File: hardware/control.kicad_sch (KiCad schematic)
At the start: 8 parts, among them U1 STM32G0C1KCTxN

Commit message: values-correction
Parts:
- C1, C3: value 100nF -> 100n
- C6: value 10uF -> 10u
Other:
- note removed: "MISO MOSI SCK? PWM: PWM1-TIM_CH3, PWM2-TIM_CH4? LED?"
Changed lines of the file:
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@@
-		)
-	)
-	(text "MISO MOSI SCK?\nPWM: PWM1-TIM_CH3, PWM2-TIM_CH4?\nLED?"
-		(exclude_from_sim no)
-		(at 193.04 88.646 0)
-		(effects
-			(font
-				(size 1.27 1.27)
-			)
 		)
 	)
@@
 			)
 		)
-		(property "Value" "10uF"
+		(property "Value" "10u"
 			(at 73.66 50.8063 0)
 			(effects
@@
 			)
 		)
-		(property "Value" "100nF"
+		(property "Value" "100n"
 			(at 85.09 50.8063 0)
 			(effects
@@
 			)
 		)
-		(property "Value" "100nF"
+		(property "Value" "100n"
 			(at 110.49 50.8062 0)
 			(effects

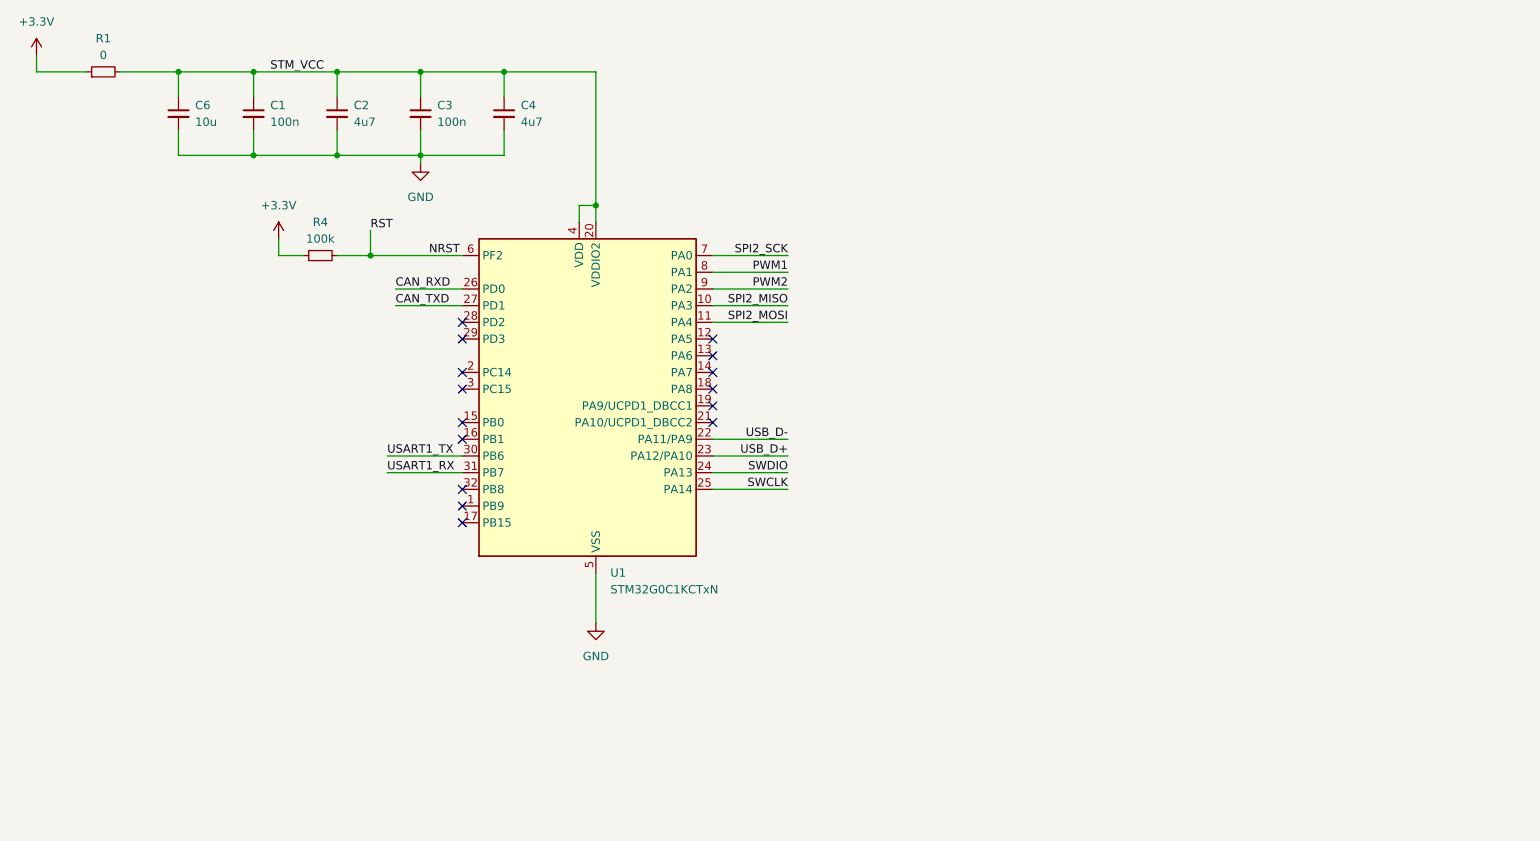
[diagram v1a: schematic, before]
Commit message: added sheet pins
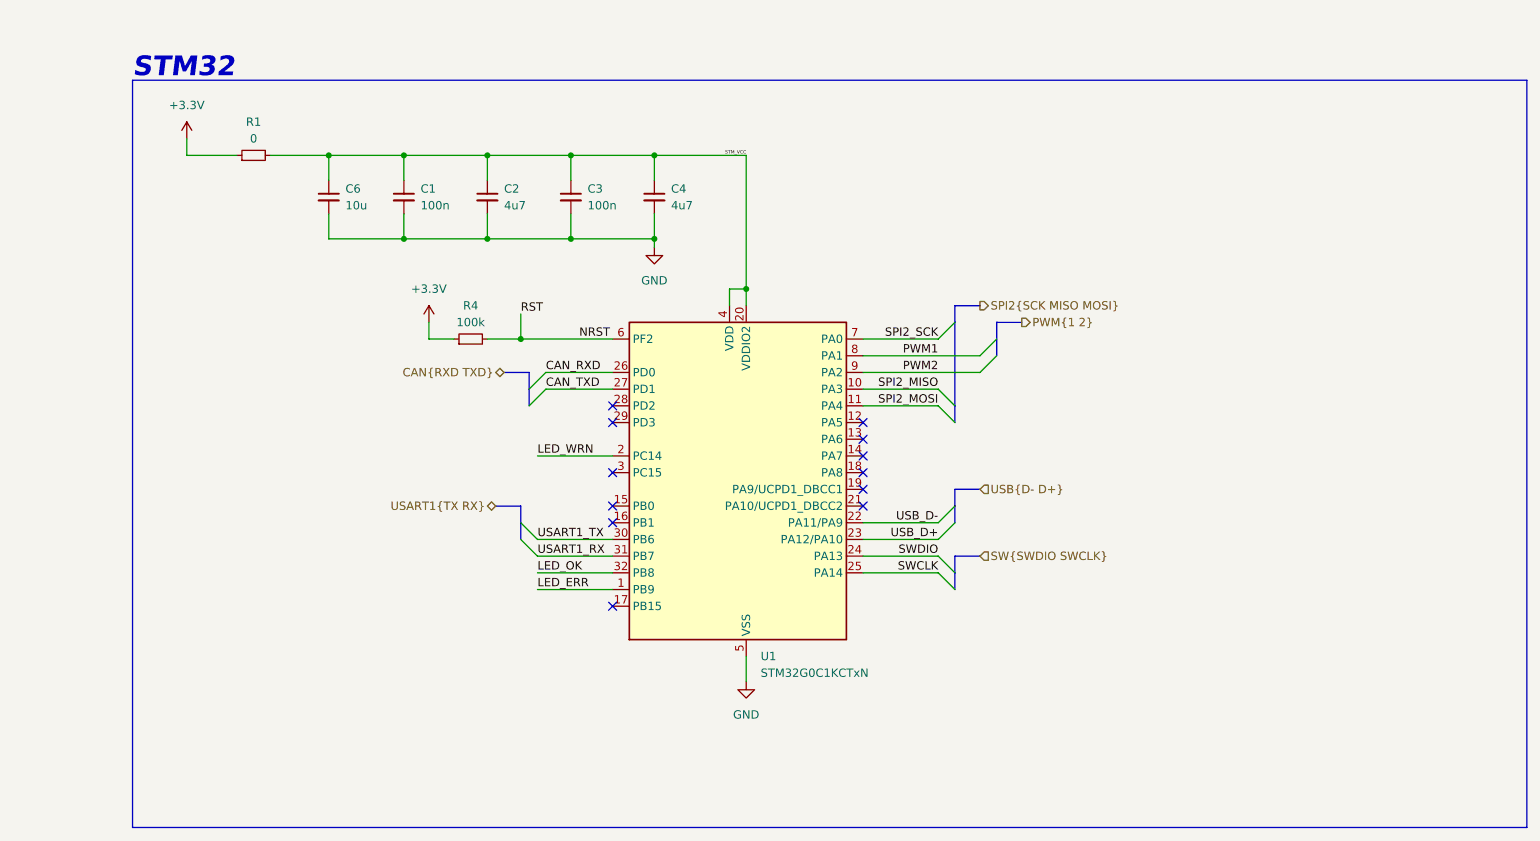
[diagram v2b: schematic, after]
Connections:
- net LED_ERR: now reaches U1.1 (PB9)
- net LED_WRN: now reaches U1.2 (PC14)
- net LED_OK: now reaches U1.32 (PB8)
- no-connect marks 15 -> 12
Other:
- note added: "STM32"
- moved on the sheet: C1, C2, C3, C4, C6, R1, R4, U1

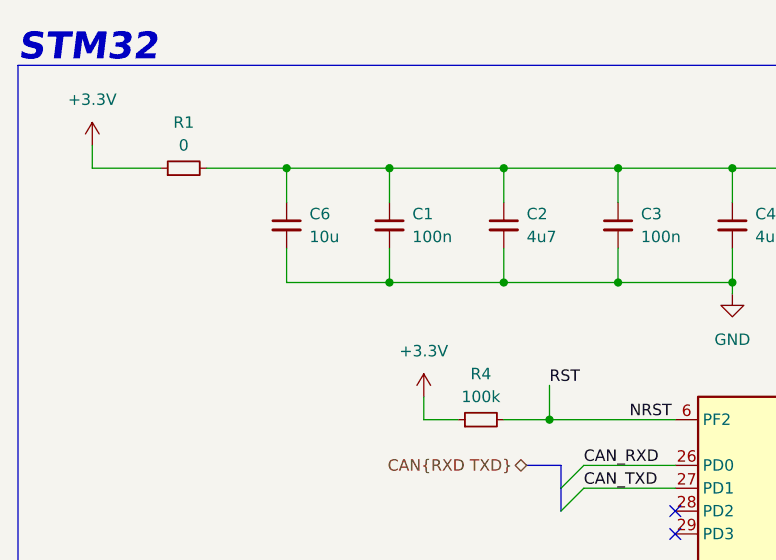
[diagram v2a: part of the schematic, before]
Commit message: connectors - added, buses - todo
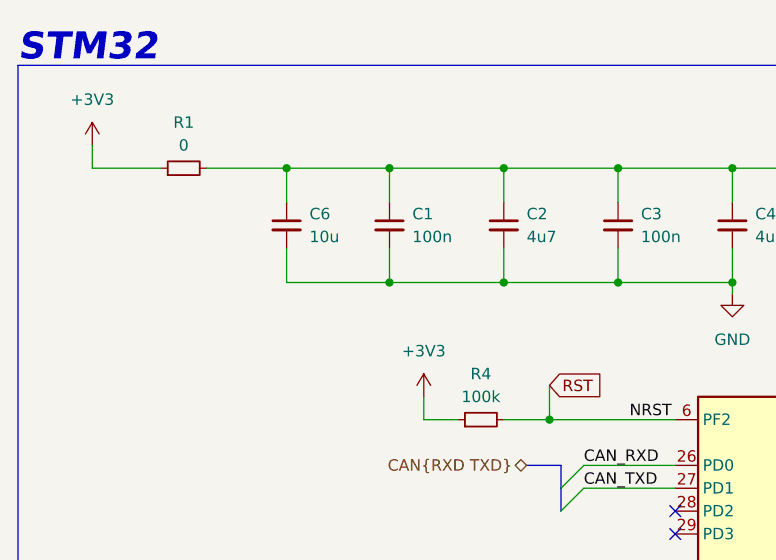
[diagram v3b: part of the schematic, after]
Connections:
- net +3.3V renamed +3V3
- net NRST renamed RST
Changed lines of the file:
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@@
-		)
-	)
-	(label "RST"
-		(at 123.19 80.01 0)
-		(fields_autoplaced yes)
-		(effects
-			(font
-				(size 1.27 1.27)
-			)
-			(justify left bottom)
 		)
 	)
@@
 			)
 			(justify right bottom)
+		)
+	)
+	(global_label "RST"
+		(shape input)
+		(at 123.19 80.01 0)
+		(fields_autoplaced yes)
+		(effects
+			(font
+				(size 1.27 1.27)
+			)
+			(justify left)
+		)
+		(property "Intersheetrefs" "${INTERSHEET_REFS}"
+			(at 129.6223 80.01 0)
+			(effects
+				(font
+					(size 1.27 1.27)
+				)
+				(justify left)
+				(hide yes)
+			)
 		)
 	)
@@
 	)
 	(symbol
-		(lib_id "power:+3.3V")
+		(lib_id "power:+3V3")
 		(at 72.39 53.34 0)
 		(unit 1)
@@
 		(dnp no)
 		(fields_autoplaced yes)
-		(property "Reference" "#PWR02"
+		(property "Reference" "#PWR029"
 			(at 72.39 57.15 0)
 			(effects
@@
 			)
 		)
-		(property "Value" "+3.3V"
+		(property "Value" "+3V3"
 			(at 72.39 48.26 0)
 			(effects
@@
 			)
 		)
-		(property "Description" ""
+		(property "Description" "Power symbol creates a global label with name \"+3V3\""
 			(at 72.39 53.34 0)
 			(effects
@@
 			(project "drs"
 				(path "/b652b05a-4e3d-4ad1-b032-18886abe7d45/5a98a3dd-0349-471b-8829-e40d62018b04"
-					(reference "#PWR02")
+					(reference "#PWR029")
 					(unit 1)
 				)
@@
 	)
 	(symbol
-		(lib_id "power:+3.3V")
+		(lib_id "power:+3V3")
 		(at 109.22 81.28 0)
 		(unit 1)
@@
 		(dnp no)
 		(fields_autoplaced yes)
-		(property "Reference" "#PWR07"
+		(property "Reference" "#PWR02"
 			(at 109.22 85.09 0)
 			(effects
@@
 			)
 		)
-		(property "Value" "+3.3V"
+		(property "Value" "+3V3"
 			(at 109.22 76.2 0)
 			(effects
@@
 			)
 		)
-		(property "Description" ""
+		(property "Description" "Power symbol creates a global label with name \"+3V3\""
 			(at 109.22 81.28 0)
 			(effects
@@
 			(project "drs"
 				(path "/b652b05a-4e3d-4ad1-b032-18886abe7d45/5a98a3dd-0349-471b-8829-e40d62018b04"
-					(reference "#PWR07")
+					(reference "#PWR02")
 					(unit 1)
 				)

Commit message: Poprawione busy, brak errorow
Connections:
- net CAN_RXD renamed RXD
- net CAN_TXD renamed TXD
- net PWM1 renamed 1
- net PWM2 renamed 2
- net SPI2_MISO renamed MISO
- net SPI2_MOSI renamed MOSI
- net SPI2_SCK renamed SCK
- net SWCLK renamed CLK
- net SWDIO renamed DIO
- net USART1_RX renamed RX
- net USART1_TX renamed TX
- net USB_D+ renamed D+
- net USB_D- renamed D-
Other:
- moved on the sheet: C1, C2, C3, C4, C6, R1, R4, U1

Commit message: Footprints addes beside PWM connectors
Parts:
- C1, C2, C3, C4, C6: footprint Capacitor_SMD:C_0603_1608Metric -> Capacitor_SMD:C_0603_1608Metric_Pad1.08x0.95mm_HandSolder
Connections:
- net 1 renamed PWM1
- net 2 renamed PWM2
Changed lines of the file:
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@@
 	)
 	(bus_alias "PWM"
-		(members "1" "2")
+		(members "PWM1" "PWM2")
 	)
 	(bus_alias "SPI"
@@
 	(label "CLK"
 		(at 173.99 119.38 0)
+		(fields_autoplaced yes)
 		(effects
 			(font
@@
 		)
 	)
-	(label "1"
+	(label "PWM1"
 		(at 185.42 86.36 180)
 		(fields_autoplaced yes)
@@
 	(label "D-"
 		(at 173.99 111.76 0)
+		(fields_autoplaced yes)
 		(effects
 			(font
@@
 		)
 	)
-	(label "2"
+	(label "PWM2"
 		(at 185.42 88.9 180)
 		(fields_autoplaced yes)
@@
 	(label "D+"
 		(at 173.99 114.3 0)
+		(fields_autoplaced yes)
 		(effects
 			(font
@@
 	(label "DIO"
 		(at 173.99 116.84 0)
+		(fields_autoplaced yes)
 		(effects
 			(font
@@
 	)
 	(hierarchical_label "{SPI}"
-		(shape input)
+		(shape bidirectional)
 		(at 198.12 78.74 0)
 		(fields_autoplaced yes)
@@
 	)
 	(hierarchical_label "{PWM}"
-		(shape input)
+		(shape output)
 		(at 204.47 86.36 0)
 		(fields_autoplaced yes)
@@
 	)
 	(hierarchical_label "{SW}"
-		(shape input)
+		(shape bidirectional)
 		(at 198.12 116.84 0)
 		(fields_autoplaced yes)
@@
 	)
 	(hierarchical_label "{USB}"
-		(shape input)
+		(shape output)
 		(at 198.12 106.68 0)
 		(fields_autoplaced yes)
@@
 	)
 	(hierarchical_label "{USART1}"
-		(shape input)
+		(shape bidirectional)
 		(at 113.03 109.22 180)
 		(fields_autoplaced yes)
@@
 			)
 		)
-		(property "Footprint" "Capacitor_SMD:C_0603_1608Metric"
+		(property "Footprint" "Capacitor_SMD:C_0603_1608Metric_Pad1.08x0.95mm_HandSolder"
 			(at 92.71 62.23 0)
 			(effects
@@
 			)
 		)
-		(property "Footprint" "Capacitor_SMD:C_0603_1608Metric"
+		(property "Footprint" "Capacitor_SMD:C_0603_1608Metric_Pad1.08x0.95mm_HandSolder"
 			(at 104.14 62.23 0)
 			(effects
@@
 			)
 		)
-		(property "Value" "PWR_FLAG"
+		(property "Value" "3V3_FLAG"
 			(at 87.63 50.8 0)
 			(effects
@@
 			)
 		)
-		(property "Footprint" "Capacitor_SMD:C_0603_1608Metric"
+		(property "Footprint" "Capacitor_SMD:C_0603_1608Metric_Pad1.08x0.95mm_HandSolder"
 			(at 116.84 62.23 0)
 			(effects
@@
 			)
 		)
-		(property "Footprint" "Capacitor_SMD:C_0603_1608Metric"
+		(property "Footprint" "Capacitor_SMD:C_0603_1608Metric_Pad1.08x0.95mm_HandSolder"
 			(at 129.54 62.23 0)
 			(effects
@@
 			)
 		)
-		(property "Footprint" "Capacitor_SMD:C_0603_1608Metric"
+		(property "Footprint" "Capacitor_SMD:C_0603_1608Metric_Pad1.08x0.95mm_HandSolder"
 			(at 142.24 62.23 0)
 			(effects

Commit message: Table updated- fuses and conns still not added
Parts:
- C1, C3: Mouser Price/Stock (none) -> https://www.mouser.pl/ProductDetail/KEMET/C0603C104J5RACTM?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
- C2, C4: Mouser Price/Stock (none) -> https://www.mouser.pl/ProductDetail/TAIYO-YUDEN/MLASG168BB5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
- C6: Mouser Price/Stock (none) -> https://www.mouser.pl/ProductDetail/Murata-Electronics/GRM1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
- R1: Mouser Price/Stock (none) -> https://www.mouser.pl/ProductDetail/Vishay-Dale/CRCW0603000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
- R4: Mouser Price/Stock (none) -> https://www.mouser.pl/ProductDetail/KOA-Speer/RK73B1JTTD104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
- U1: Mouser Price/Stock (none) -> https://www.mouser.pl/ProductDetail/STMicroelectronics/STM3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
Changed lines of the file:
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@@
 			)
 		)
-		(property "Datasheet" "~"
+		(property "Datasheet" "https://www.mouser.pl/datasheet/2/281/1/GRM188R6YA106MA73_01A-1985794.pdf"
 			(at 92.71 62.23 0)
 			(effects
@@
 		)
 		(property "m" "C0603C104K5RAC3121"
+			(at 92.71 62.23 0)
+			(effects
+				(font
+					(size 1.27 1.27)
+				)
+				(hide yes)
+			)
+		)
+		(property "Mouser Price/Stock" "https://www.mouser.pl/ProductDetail/Murata-Electronics/GRM188R6YA106MA73J?qs=5aG0NVq1C4xLSwNPdfnaYg%3D%3D"
 			(at 92.71 62.23 0)
 			(effects
@@
 			)
 		)
+		(property "Mouser Price/Stock" "https://www.mouser.pl/ProductDetail/STMicroelectronics/STM32G0C1KCT6N?qs=iLbezkQI%252Bshu4f%252BBp0CpFw%3D%3D"
+			(at 153.67 106.68 0)
+			(effects
+				(font
+					(size 1.27 1.27)
+				)
+				(hide yes)
+			)
+		)
 		(pin "20"
 		)
@@
 			)
 		)
-		(property "Datasheet" "~"
+		(property "Datasheet" "https://www.mouser.pl/datasheet/2/447/KEM_C1002_X7R_SMD-3316098.pdf"
 			(at 104.14 62.23 0)
 			(effects
@@
 		)
 		(property "m" "C0603C104K5RAC3121"
+			(at 104.14 62.23 0)
+			(effects
+				(font
+					(size 1.27 1.27)
+				)
+				(hide yes)
+			)
+		)
+		(property "Mouser Price/Stock" "https://www.mouser.pl/ProductDetail/KEMET/C0603C104J5RACTM?qs=JHaSZE6YWYWxKFeO4jSa6A%3D%3D"
 			(at 104.14 62.23 0)
 			(effects
@@
 			)
 		)
-		(property "Datasheet" "~"
+		(property "Datasheet" "https://www.koaspeer.com/pdfs/RK73B.pdf"
 			(at 114.3 83.82 0)
 			(effects
@@
 		(property "Mouser" "https://www.mouser.pl/ProductDetail/KOA-Speer/RK73Z1JTTDD?qs=sGAEpiMZZMtlubZbdhIBIOIkEhSyZ1IOpjyUKjVzbOA%3D"
 			(at 114.3 83.82 90)
+			(effects
+				(font
+					(size 1.27 1.27)
+				)
+				(hide yes)
+			)
+		)
+		(property "Mouser Price/Stock" "https://www.mouser.pl/ProductDetail/KOA-Speer/RK73B1JTTD104J?qs=sGAEpiMZZMvdGkrng054t2HaaJFon%252B0pQ1vDU7rpyKc%3D"
+			(at 114.3 83.82 0)
 			(effects
 				(font
@@
 			)
 		)
-		(property "Datasheet" "~"
+		(property "Datasheet" "https://www.mouser.pl/datasheet/2/396/ML_mlcc_all_e-3369844.pdf"
 			(at 116.84 62.23 0)
 			(effects
@@
 		)
 		(property "m" "CL10A475KQ8NNNL"
+			(at 116.84 62.23 0)
+			(effects
+				(font
+					(size 1.27 1.27)
+				)
+				(hide yes)
+			)
+		)
+		(property "Mouser Price/Stock" "https://www.mouser.pl/ProductDetail/TAIYO-YUDEN/MLASG168BB5475KTNA01?qs=tlsG%2FOw5FFhCGJXg7RRAyQ%3D%3D"
 			(at 116.84 62.23 0)
 			(effects
@@
 			)
 		)
-		(property "Datasheet" "~"
+		(property "Datasheet" "https://www.mouser.pl/datasheet/2/447/KEM_C1002_X7R_SMD-3316098.pdf"
 			(at 129.54 62.23 0)
 			(effects
@@
 		)
 		(property "m" "C0603C104K5RAC3121"
+			(at 129.54 62.23 0)
+			(effects
+				(font
+					(size 1.27 1.27)
+				)
+				(hide yes)
+			)
+		)
+		(property "Mouser Price/Stock" "https://www.mouser.pl/ProductDetail/KEMET/C0603C104J5RACTM?qs=JHaSZE6YWYWxKFeO4jSa6A%3D%3D"
 			(at 129.54 62.23 0)
 			(effects
@@
 			)
 		)
-		(property "Datasheet" "~"
+		(property "Datasheet" "https://www.mouser.pl/datasheet/2/396/ML_mlcc_all_e-3369844.pdf"
 			(at 142.24 62.23 0)
 			(effects
@@
 		)
 		(property "m" "CL10A475KQ8NNNL"
+			(at 142.24 62.23 0)
+			(effects
+				(font
+					(size 1.27 1.27)
+				)
+				(hide yes)
+			)
+		)
+		(property "Mouser Price/Stock" "https://www.mouser.pl/ProductDetail/TAIYO-YUDEN/MLASG168BB5475KTNA01?qs=tlsG%2FOw5FFhCGJXg7RRAyQ%3D%3D"
 			(at 142.24 62.23 0)
 			(effects
@@
 			)
 		)
-		(property "Datasheet" "~"
+		(property "Datasheet" "https://www.vishay.com/docs/20035/dcrcwe3.pdf"
 			(at 81.28 55.88 0)
 			(effects
@@
 			(effects
 				(font
+					(size 1.27 1.27)
+				)
+				(hide yes)
+			)
+		)
+		(property "Mouser Price/Stock" "https://www.mouser.pl/ProductDetail/Vishay-Dale/CRCW06030000Z0ED?qs=sGAEpiMZZMtlubZbdhIBIKbhzOdzan%2FGQpe36dKZ2cw%3D"
+			(at 81.28 55.88 0)
+			(effects
+				(font
